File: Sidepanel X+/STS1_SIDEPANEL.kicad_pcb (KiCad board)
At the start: 4 copper layers, 98 x 98 mm, 45 parts, among them J1 Conn_01x10, J3 Conn_02x02_Odd_Even, U11 INA180A4, U12 INA180A4

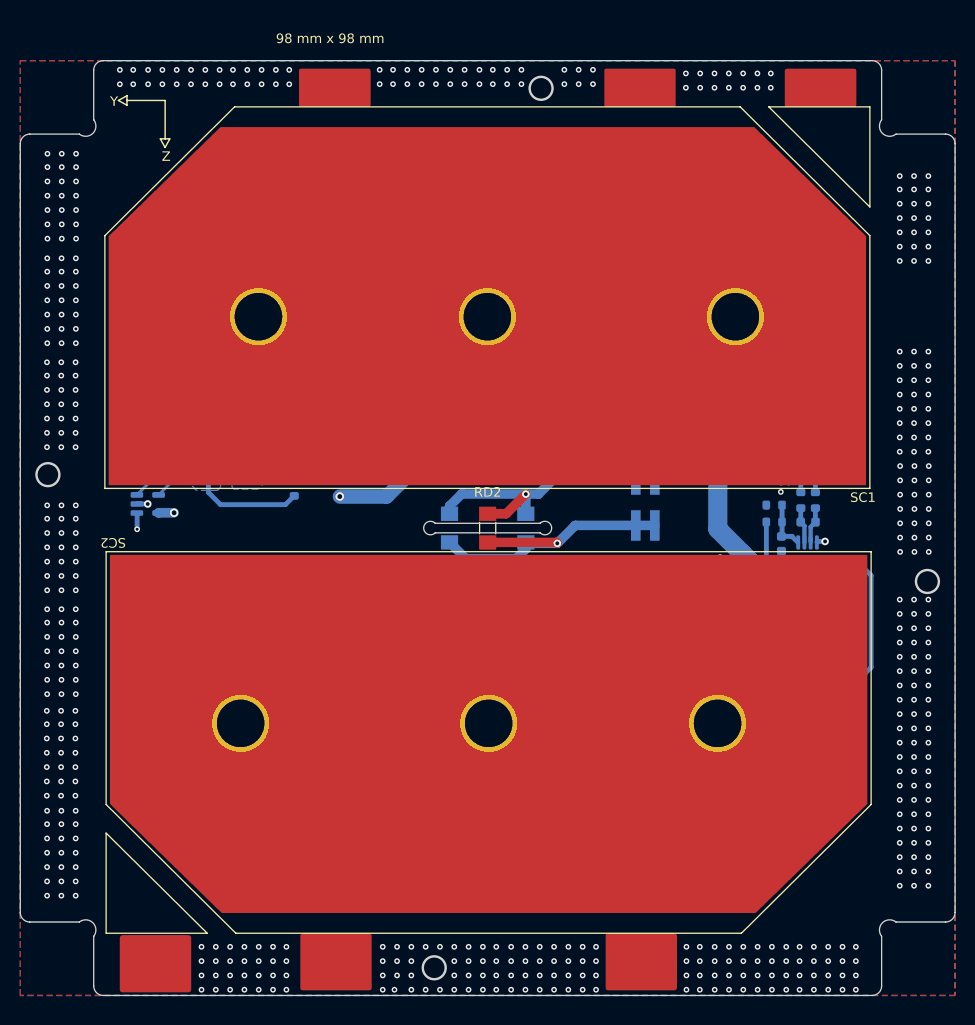
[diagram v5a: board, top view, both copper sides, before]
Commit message: moved the connectors, changed the footprint of the input and output capacitors and splitted the input capacitor in two
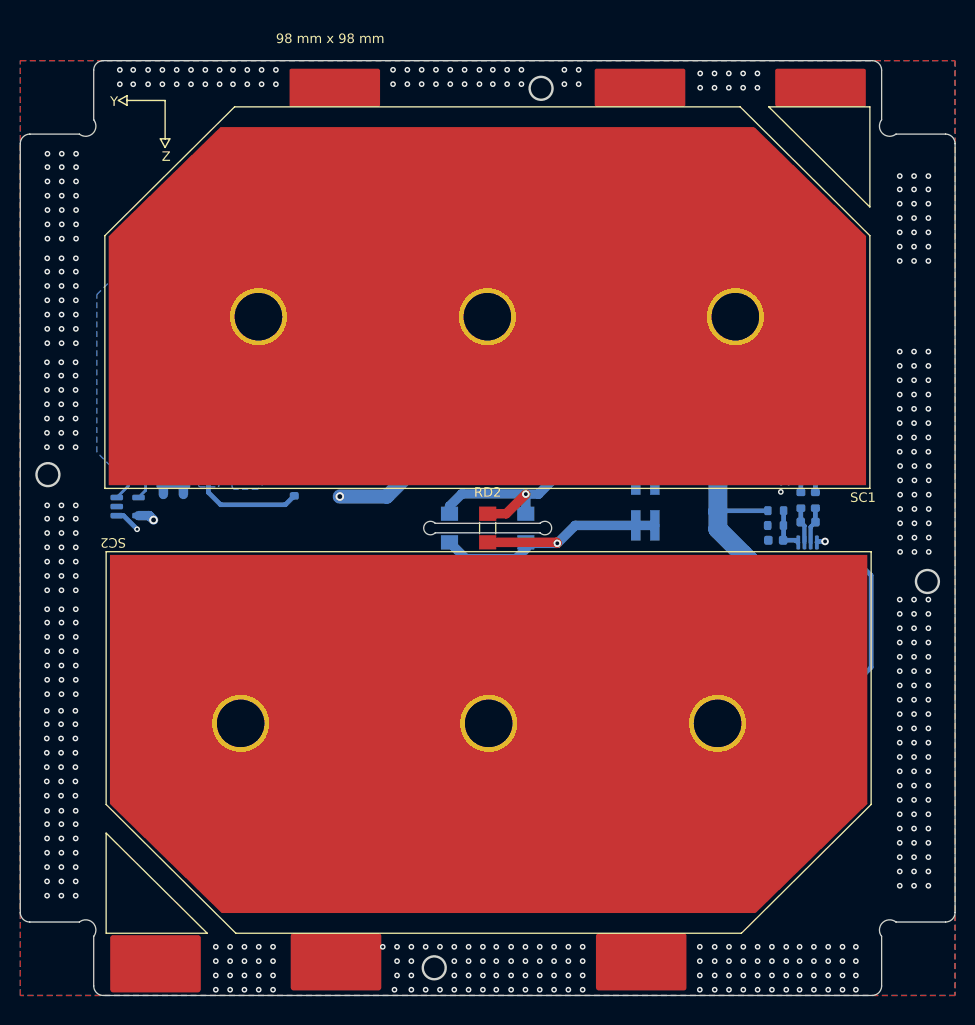
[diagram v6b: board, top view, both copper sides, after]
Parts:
- C11, C12, C61, C62: value 10u -> 22u; footprint Capacitor_SMD:C_0603_1608Metric -> Capacitor_SMD:C_0805_2012Metric
- C21, C22: value 100n -> 1n
- C41: value 4u7 -> 1u
- C51: value 1u -> 22u; footprint Capacitor_SMD:C_0603_1608Metric -> Capacitor_SMD:C_0805_2012Metric
- C52: value 4u7 -> 22u; footprint Capacitor_SMD:C_0603_1608Metric -> Capacitor_SMD:C_0805_2012Metric
- R11, R12: footprint Resistor_SMD:R_0603_1608Metric -> Resistor_SMD:R_0805_2012Metric
- R51, R52: value 0R01 -> 220m; footprint Resistor_SMD:R_0603_1608Metric -> Resistor_SMD:R_0805_2012Metric
- R61: value 1M -> 3k
- R71: value 330k -> 1k
- moved C61 17.2 mm to (93.1, 84.0), turned to -90 degrees
- moved C62 16.2 mm to (156.6, 109.1)
- moved C51 11.3 mm to (101.3, 75.2), turned to 180 degrees
- moved C41 11.3 mm to (111.4, 80.3), turned to -90 degrees
- moved C11 8.23 mm to (91.0, 83.9), turned to -90 degrees
- moved R11 3.98 mm to (88.2, 81.9)
- moved R12 3.96 mm to (157.4, 111.9)
- moved C12 3.11 mm to (156.6, 107.0)
- moved R72 2.14 mm to (155.2, 89.2)
- moved U11 2.13 mm to (87.2, 87.2)
- moved D22 2.09 mm to (149.9, 97.3), turned to 180 degrees
- moved R71 1.68 mm to (110.9, 76.6)
- moved R61 1.63 mm to (112.5, 76.6)
- moved C31 1.50 mm to (109.3, 76.6), turned to 90 degrees
- moved U12 1.34 mm to (161.6, 112.5)
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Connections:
- C41 pad 1: /SolarMPPT/MPPT1_OUT -> Net-(MPPT1-ICTRL_MINUS)
- C41 pad 2: GND -> Net-(MPPT1-ICTRL_PLUS)
- C51 pad 1: Net-(MPPT1-ICTRL_MINUS) -> /SolarMPPT/MPPT1_OUT
- C51 pad 2: Net-(MPPT1-ICTRL_PLUS) -> GND
- C61 pad 1: /MPPT1 -> /SolarMPPT/CUR1_OUT
- C62 pad 1: /MPPT2 -> /SolarMPPT/CUR2_OUT
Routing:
- net /SC1_V+: track 47.8 -> 19.5 mm
- net /MPPT2: track 77.8 -> 81.1 mm
- net GND: track 21.7 -> 24.7 mm, vias 703 -> 672
- net /MPPT1: track 88.1 -> 90.0 mm
- net /SC2_V+: track 45.9 -> 44.7 mm
- net /SC1_I+: track 53.7 -> 54.7 mm
- net /SolarMPPT/CUR2_OUT: track 21.9 -> 21.2 mm
- net /SolarMPPT/CUR1_OUT: track 18.9 -> 18.2 mm
- net /SC2_I+: track 54.5 -> 55.1 mm
- net Net-(MPPT2-VCTRL): track 5.30 -> 4.77 mm

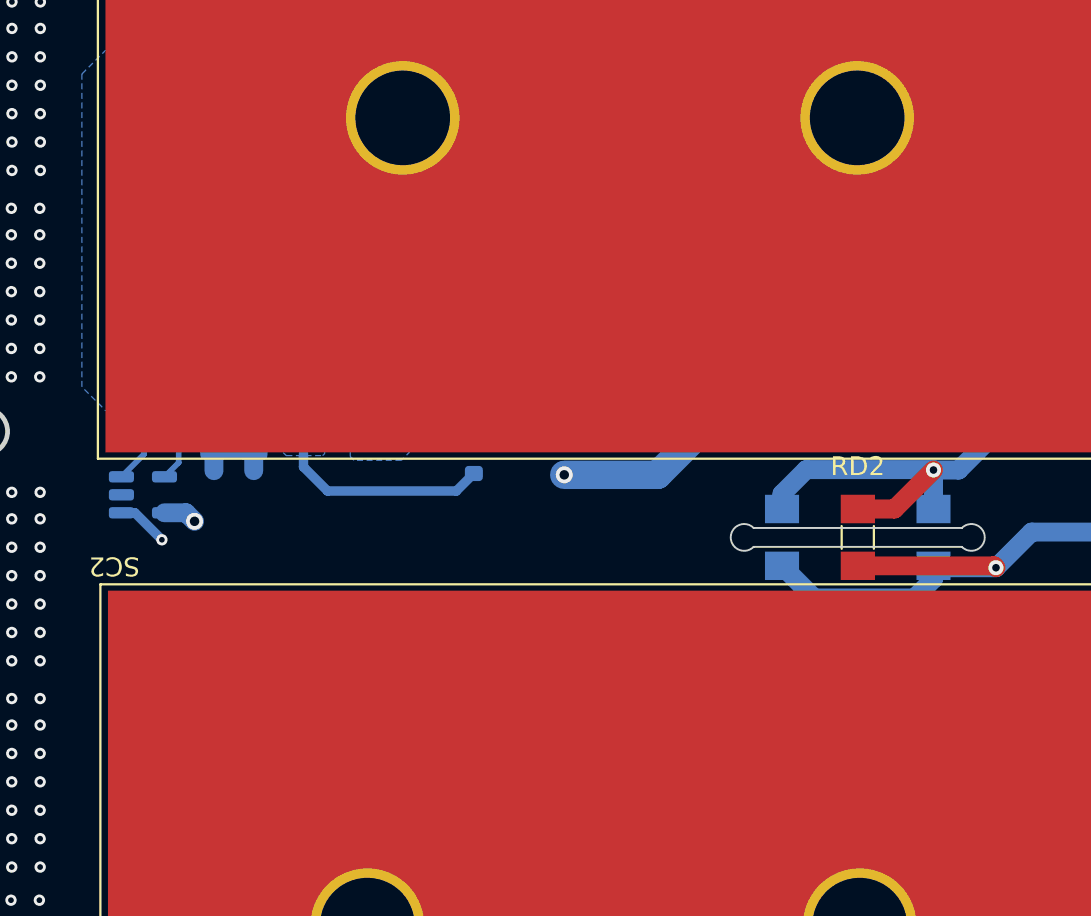
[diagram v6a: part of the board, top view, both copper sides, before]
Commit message: small change in the routing
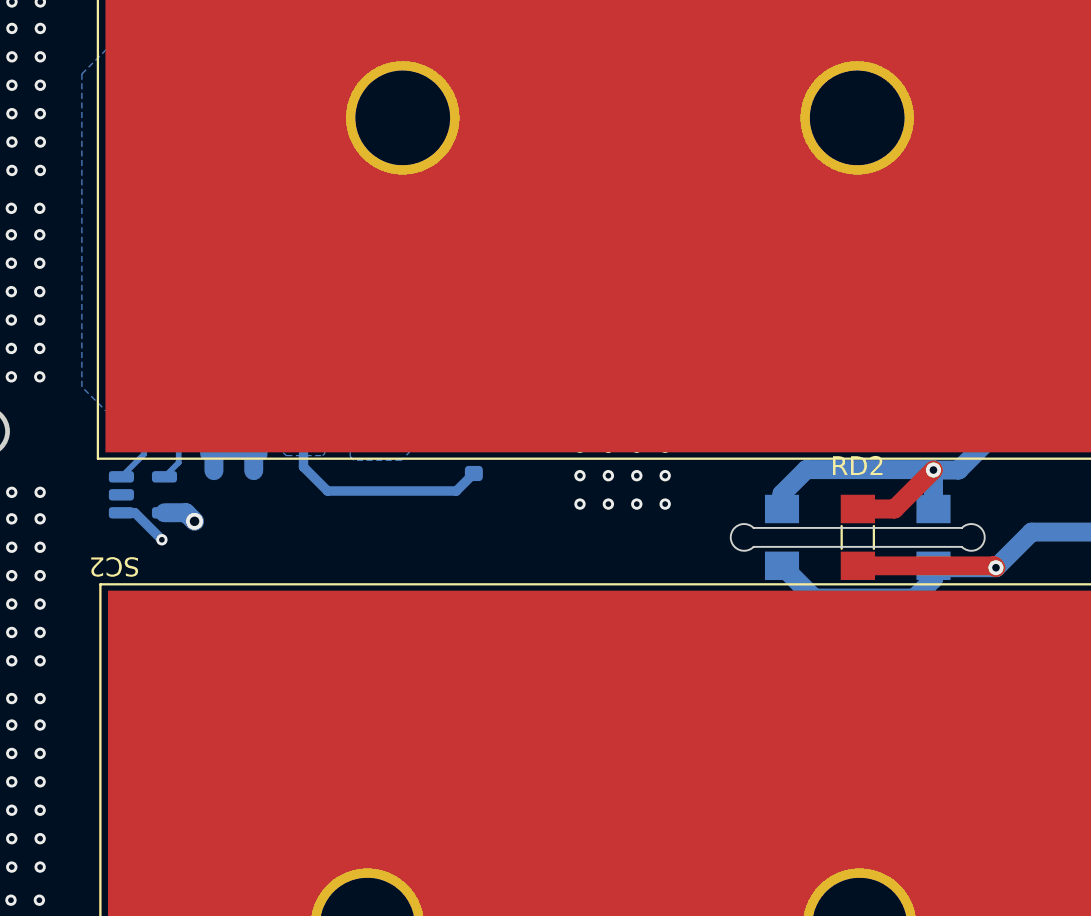
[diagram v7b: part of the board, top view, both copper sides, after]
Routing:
- net /MPPT1: track 90.0 -> 75.7 mm, vias 4 -> 3
- net GND: vias 672 -> 684
- net /SC1_V+: vias 0 -> 1
